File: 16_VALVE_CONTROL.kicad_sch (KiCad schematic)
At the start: 36 parts, among them U7 74HC595, U8 74HC595

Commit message: finish some unconnect pins, draw edge cut board
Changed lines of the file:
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@@
 		(property "Reference" "U8"
 			(at 144.8944 32.385 0)
+			(show_name yes)
 			(effects
 				(font
@@
 		(property "Value" "74HC595"
 			(at 144.8944 34.925 0)
+			(show_name yes)
 			(effects
 				(font

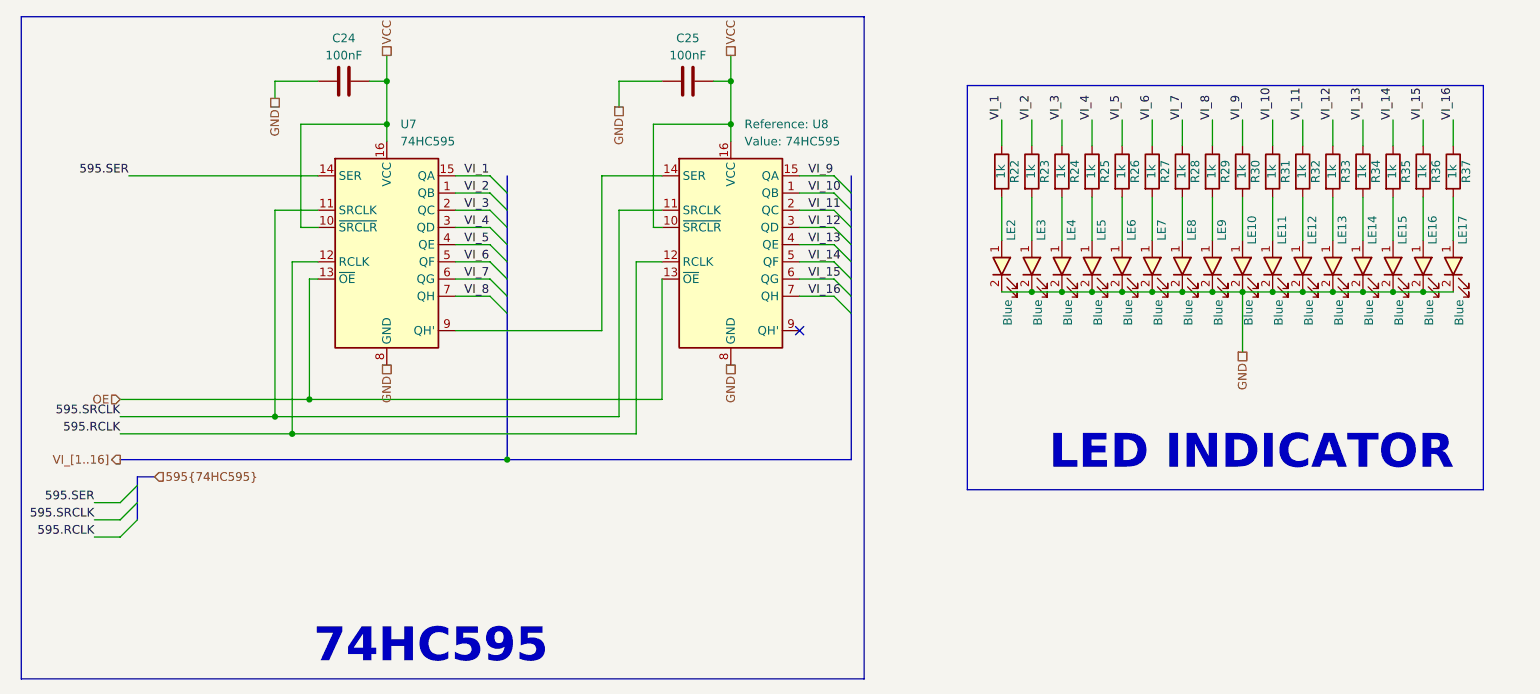
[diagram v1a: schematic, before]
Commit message: Add LORA, SDcard and Volt to 4_20mA scheamtic
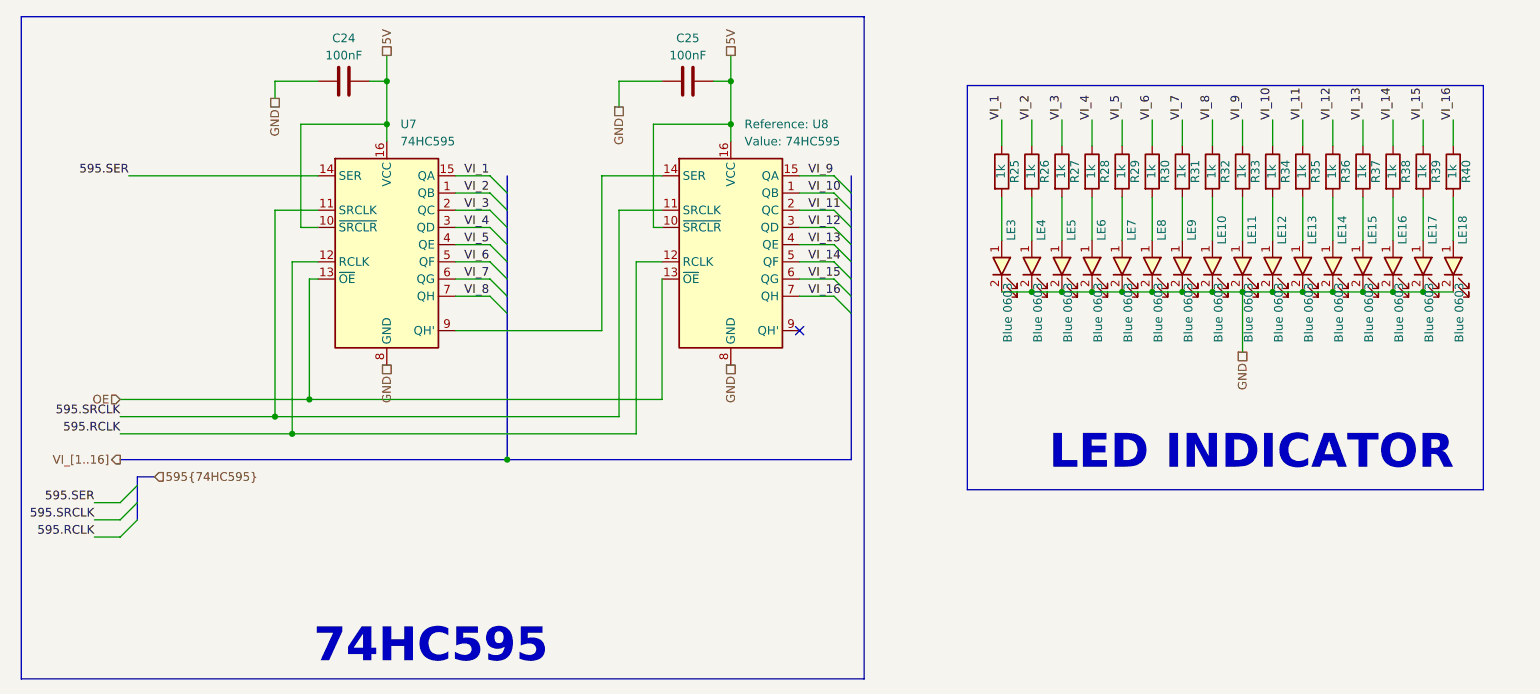
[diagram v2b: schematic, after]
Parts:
- LE10: renamed from LE9; value Blue -> Blue 0603
- LE11: renamed from LE10; value Blue -> Blue 0603
- LE12: renamed from LE11; value Blue -> Blue 0603
- LE13: renamed from LE12; value Blue -> Blue 0603
- LE14: renamed from LE13; value Blue -> Blue 0603
- LE15: renamed from LE14; value Blue -> Blue 0603
- LE16: renamed from LE15; value Blue -> Blue 0603
- LE17: renamed from LE16; value Blue -> Blue 0603
- LE18: renamed from LE17; value Blue -> Blue 0603
- LE3: renamed from LE2; value Blue -> Blue 0603
- LE4: renamed from LE3; value Blue -> Blue 0603
- LE5: renamed from LE4; value Blue -> Blue 0603
- LE6: renamed from LE5; value Blue -> Blue 0603
- LE7: renamed from LE6; value Blue -> Blue 0603
- LE8: renamed from LE7; value Blue -> Blue 0603
- LE9: renamed from LE8; value Blue -> Blue 0603
- renumbered R22 to R25, R23 to R26, R24 to R27, R25 to R28, R26 to R29, R27 to R30, R28 to R31, R29 to R32, R30 to R33, R31 to R34, R32 to R35, R33 to R36, R34 to R37, R35 to R38, R36 to R39, R37 to R40
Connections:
- net VCC renamed 5V
